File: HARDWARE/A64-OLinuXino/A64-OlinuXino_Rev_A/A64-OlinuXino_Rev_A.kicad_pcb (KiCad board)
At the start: 6 copper layers, 90 x 62.5 mm, 396 parts, among them Q1 E4SB25.000F20E15(25MHz/20pF/2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, Q2 MC-306_32.768KHZ/SMD_8038/6pF, Q3 4SB24.000F20E15/5x3.2mm/20ppm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, T1 WPM1481(DFN2X2-6L), U1 AllWinner-A64(FBGA396), U10 NA(RCLAMP0524P(SLP2510P8)), U11 RTL8723BS(ComboModule), U12 RTL8211CL-GR(LQFP48), U13 MT3608(SOT23-6), U14 AXP803(QFN68_8x8mm), U15 AT24C16BN-SH(SO-8_150mil), U2 K4B4G1646D-BCK0(FBGA-96_256Mx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, U3 K4B4G1646D-BCK0(FBGA-96_256Mx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, U4 NA(H27UBG8T2BTR-BC(TSOP48)), U5 MTFC4GACAANA-4M_IT(TBGA100), U6 SY6280AAC(SOT23-5), U7 NA(RCLAMP0524P(SLP2510P8)), U8 NA(RCLAMP0524P(SLP2510P8)), U9 SY6280AAC(SOT23-5)

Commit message: A64-OLinuXino update
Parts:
- removed C196: 100nF, OLIMEX_RLC-FP:C_0402_5MIL_DWS
- removed CON: B4B-PH-K-S, OLIMEX_Connectors-FP:B4B-PH-K-S
- removed Case: Case_Value, OLIMEX_Cases-FP:HAMMOND_1593LBK_A10_LIME
- removed R100, R99: NA(2.2k), OLIMEX_RLC-FP:R_0402_5MIL_DWS
- removed RM8: RA1206_(4x0603)_4B8_22R, OLIMEX_RLC-FP:RA1206_(4X0603)_4B8_xx
- removed U15: AT24C16BN-SH(SO-8_150mil), OLIMEX_IC-FP:SO-8
- added C197: 100nF, OLIMEX_RLC-FP:C_0402_5MIL_DWS, B.Cu at (143.7, 70.2)
- added HSIC1: B4B-PH-K-S, OLIMEX_Connectors-FP:B4B-PH-K-S, F.Cu at (121.8, 45.0)
- added HSIC_E1: Opened, OLIMEX_Jumpers-FP:SJ, B.Cu at (119.5, 47.4)
- added R101: NA(2.2k), OLIMEX_RLC-FP:R_0402_5MIL_DWS, F.Cu at (154.6, 64.4)
- added R102: NA(2.2k), OLIMEX_RLC-FP:R_0402_5MIL_DWS, F.Cu at (154.6, 63.4)
- added R103: NA(100k), OLIMEX_RLC-FP:R_0402_5MIL_DWS, B.Cu at (125.3, 46.9)
- added R104: NA(10k), OLIMEX_RLC-FP:R_0402_5MIL_DWS, B.Cu at (124.5, 46.9)
- 5V_E1, C1, C10, C102, C103, C104, C109, C11, C110, C113, C114, C115, C116, C117, C118, C119, C12, C120, C121, C123, C125, C126, C127, C128, C13, C130, C132, C133, C134, C135, C137, C14, C142, C145, C148, C149, C15, C151, C152, C153, C155, C156, C157, C158, C159, C16, C160, C161, C162, C163, C164, C165, C166, C167, C168, C17, C170, C171, C173, C174, C176, C177, C178, C179, C18, C180, C181, C183, C184, C186, C188, C189, C19, C190, C191, C192, C194, C195, C2, C20, C21, C22, C23, C24, C25, C26, C27, C28, C29, C3, C30, C31, C34, C35, C36, C37, C38, C4, C42, C43, C44, C46, C49, C5, C50, C51, C53, C54, C55, C56, C6, C61, C63, C64, C7, C72, C73, C79, C8, C80, C82, C88, C9, C96, C98, C99, D1, D3, D4, EMMC_PWR1, FET1, FET2, FUSE1, FUSE2, L1, L13, L2, Q1, Q2, R2, R3, R36, R37, R38, R4, R41, R42, R60, R61, R93, R96, R97, RM1, RM10, RM12, RM14, RM2, RM3, RM4, RM5, RM7, T1, VCC-PE:2.8V/3.3V1: moved to B.Cu
- NAND_E1: value Closed -> Soldered; moved to B.Cu
- PWRON1, RESET1, UBOOT1: footprint OLIMEX_Buttons-FP:WS_TAKT_6X3,5_SMD_NOCREAM -> OLIMEX_Buttons-FP:uTACTIL
- R1, R10, R11, R12, R14, R16, R17, R19, R20, R22, R24, R25, R26, R27, R28, R29, R32, R34, R35, R47, R48, R49, R50, R51, R52, R53, R55, R56, R57, R6, R63, R64, R65, R67, R7, R80, R81: footprint OLIMEX_RLC-FP:R_0603_5MIL_DWS -> OLIMEX_RLC-FP:R_0402_5MIL_DWS
- R13, R15, R21, R23, R30, R31, R46, R5, R58, R59, R66, R68, R69, R70, R71, R72, R73, R75, R76, R77, R79, R8, R83, R84, R85, R86, R87, R88, R89, R9, R90, R91, R92, R95: footprint OLIMEX_RLC-FP:R_0603_5MIL_DWS -> OLIMEX_RLC-FP:R_0402_5MIL_DWS; moved to B.Cu
- R74, R82: value 1k -> 2.2k; footprint OLIMEX_RLC-FP:R_0603_5MIL_DWS -> OLIMEX_RLC-FP:R_0402_5MIL_DWS
- R78: footprint OLIMEX_RLC-FP:R_0603_5MIL_DWS -> OLIMEX_RLC-FP:R_1206_5MIL_DWS; moved to B.Cu
- UEXT1: footprint OLIMEX_Connectors-FP:GBH-254-SMT-10 -> OLIMEX_Connectors-FP:HN2x5
- moved L5 502.1 mm to (113.5, 79.8), turned to 180 degrees
- moved R31 499.2 mm to (116.8, 84.5)
- moved C64 498.6 mm to (116.7, 87.1), turned to 270 degrees
- moved L2 490.2 mm to (118.6, 87.1), turned to 90 degrees
- moved R25 487.1 mm to (112.8, 88.6), turned to 90 degrees
- moved C58 485.1 mm to (114.3, 92.1)
- moved C62 480.2 mm to (115.3, 90.9)
- moved C51 475.8 mm to (137.5, 72.1), turned to 270 degrees
- moved R28 474.1 mm to (116.8, 90.6), turned to 270 degrees
- moved R26 473.9 mm to (113.3, 90.0), turned to 180 degrees
- moved R24 471.5 mm to (136.5, 52.3), turned to 90 degrees
- moved C48 471.0 mm to (113.3, 90.9)
- moved R19 469.1 mm to (136.8, 46.8), turned to 180 degrees
- moved C52 467.3 mm to (113.8, 88.6), turned to 90 degrees
- moved C66 466.5 mm to (116.6, 71.4), turned to 270 degrees
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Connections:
- net /S0SCKN renamed /S0SCK_N
- net /S0SCKP renamed /S0SCK_P
- net /S0SDQS0N renamed /S0SDQS0_N
- net /S0SDQS0P renamed /S0SDQS0_P
- net /S0SDQS1N renamed /S0SDQS1_N
- net /S0SDQS1P renamed /S0SDQS1_P
- net /S0SDQS2N renamed /S0SDQS2_N
- net /S0SDQS2P renamed /S0SDQS2_P
- net /S0SDQS3N renamed /S0SDQS3_N
- net /S0SDQS3P renamed /S0SDQS3_P
- RM10 pad 1.1: Net-(R53-Pad2) -> Net-(RM10-Pad1.1)
- RM10 pad 3.1: Net-(RM10-Pad3.1) -> Net-(R53-Pad2)
- RM11 pad 1.1: Net-(RM11-Pad1.1) -> Net-(RM10-Pad2.1)
- RM11 pad 1.2: /USB&HDMI,WiFi&BT,Ethernet,LCD/GRXD0/LCD_D15 -> /USB&HDMI,WiFi&BT,Ethernet,LCD/GRXD2/LCD_D13
- RM11 pad 2.1: Net-(R53-Pad2) -> Net-(RM11-Pad2.1)
- RM11 pad 2.2: /USB&HDMI,WiFi&BT,Ethernet,LCD/GRXD1/LCD_D14 -> /USB&HDMI,WiFi&BT,Ethernet,LCD/GRXD0/LCD_D15
- RM11 pad 3.1: Net-(RM10-Pad2.1) -> Net-(R53-Pad2)
- RM11 pad 3.2: /USB&HDMI,WiFi&BT,Ethernet,LCD/GRXD2/LCD_D13 -> /USB&HDMI,WiFi&BT,Ethernet,LCD/GRXD1/LCD_D14
- RM11 pad 4.1: Net-(RM10-Pad3.1) -> Net-(RM10-Pad1.1)
- RM13 pad 1.1: Net-(RM10-Pad4.1) -> Net-(C88-Pad2)
- RM13 pad 1.2: /USB&HDMI,WiFi&BT,Ethernet,LCD/GRXCTL/LCD_D19 -> /USB&HDMI,WiFi&BT,Ethernet,LCD/GRXCK/LCD_D18
- RM13 pad 2.1: Net-(C88-Pad2) -> Net-(RM10-Pad4.1)
- RM13 pad 2.2: /USB&HDMI,WiFi&BT,Ethernet,LCD/GRXCK/LCD_D18 -> /USB&HDMI,WiFi&BT,Ethernet,LCD/GRXCTL/LCD_D19
- RM3 pad 1.1: /NAND Flash , eMMC, T-Card and Audio/NAND0-DQ4/SDC2-D4 -> /NAND Flash , eMMC, T-Card and Audio/NAND0-DQ7/SDC2-D7
- RM3 pad 4.1: /NAND Flash , eMMC, T-Card and Audio/NAND0-DQ7/SDC2-D7 -> /NAND Flash , eMMC, T-Card and Audio/NAND0-DQ4/SDC2-D4
- RM5 pad 1.1: /NAND Flash , eMMC, T-Card and Audio/NAND0-RE/SDC2-CLK -> (no net)
- RM5 pad 1.2: Net-(EMMC1-Pad4) -> (no net)
- RM5 pad 2.1: /NAND Flash , eMMC, T-Card and Audio/NAND0-RB0/SDC2-CMD -> /NAND Flash , eMMC, T-Card and Audio/NAND0-DQS/SDC2-RST
- RM5 pad 2.2: Net-(EMMC1-Pad6) -> Net-(EMMC1-Pad8)
- RM5 pad 3.1: /NAND Flash , eMMC, T-Card and Audio/NAND0-DQS/SDC2-RST -> /NAND Flash , eMMC, T-Card and Audio/NAND0-RE/SDC2-CLK
- RM5 pad 3.2: Net-(EMMC1-Pad8) -> Net-(EMMC1-Pad4)
- RM5 pad 4.1: (no net) -> /NAND Flash , eMMC, T-Card and Audio/NAND0-RB0/SDC2-CMD
- RM5 pad 4.2: (no net) -> Net-(EMMC1-Pad6)
- RM6 pad 3.1: (no net) -> /NAND Flash , eMMC, T-Card and Audio/HPOUTR
- RM6 pad 3.2: (no net) -> Net-(C66-Pad2)
- U12 pad 14: Net-(RM11-Pad1.1) -> Net-(RM11-Pad2.1)
- U12 pad 18: Net-(RM10-Pad3.1) -> Net-(RM10-Pad1.1)
- U14 pad 8: Net-(L19-Pad1) -> +1.5V
- U14 pad 9: Net-(L20-Pad1) -> 1.1V_SYS
- U2 pad A2: /S0SDQ13 -> /S0SDQ15
- U2 pad A3: /S0SDQ15 -> /S0SDQ12
- U2 pad A7: /S0SDQ12 -> /S0SDQ8
- U2 pad B8: /S0SDQ14 -> /S0SDQ10
- U2 pad C2: /S0SDQ11 -> /S0SDQ13
- U2 pad C3: /S0SDQ9 -> /S0SDQ14
- U2 pad C8: /S0SDQ10 -> /S0SDQ9
- U2 pad D7: /S0SDQ8 -> /S0SDQ11
- U2 pad E3: /S0SDQ0 -> /S0SDQ4
- U2 pad F7: /S0SDQ1 -> /S0SDQ0
- U2 pad F8: /S0SDQ3 -> /S0SDQ7
- U2 pad G2: /S0SDQ6 -> /S0SDQ1
- U2 pad H3: /S0SDQ4 -> /S0SDQ5
- U2 pad H7: /S0SDQ7 -> /S0SDQ3
- U2 pad H8: /S0SDQ5 -> /S0SDQ6
- U3 pad A2: /S0SDQ29 -> /S0SDQ30
- U3 pad A3: /S0SDQ31 -> /S0SDQ28
- U3 pad A7: /S0SDQ28 -> /S0SDQ24
- U3 pad B8: /S0SDQ30 -> /S0SDQ27
- U3 pad C2: /S0SDQ27 -> /S0SDQ31
- U3 pad C3: /S0SDQ25 -> /S0SDQ29
- U3 pad C8: /S0SDQ26 -> /S0SDQ25
- U3 pad D7: /S0SDQ24 -> /S0SDQ26
- U3 pad E3: /S0SDQ16 -> /S0SDQ22
- U3 pad F2: /S0SDQ18 -> /S0SDQ21
- U3 pad F7: /S0SDQ17 -> /S0SDQ16
- U3 pad G2: /S0SDQ22 -> /S0SDQ23
- U3 pad H7: /S0SDQ23 -> /S0SDQ18
- U3 pad H8: /S0SDQ21 -> /S0SDQ17
- U5 pad K9: Net-(RM3-Pad4.2) -> Net-(RM3-Pad1.2)
- U5 pad N8: Net-(RM3-Pad1.2) -> Net-(RM3-Pad4.2)
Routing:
- net GND: track 0.00 -> 259.1 mm, vias 0 -> 147
- net +5V: track 0.00 -> 79.0 mm, vias 0 -> 1
- net AP-RESET#: track 0.00 -> 75.8 mm, vias 0 -> 4
- net Net-(R86-Pad1): track 0.00 -> 66.5 mm, vias 0 -> 1
- net Net-(R87-Pad1): track 0.00 -> 66.3 mm, vias 0 -> 1
- net +1.5V: track 0.00 -> 66.1 mm, vias 0 -> 41
- net /USB&HDMI,WiFi&BT,Ethernet,LCD/BT-RST-N: track 0.00 -> 61.8 mm, vias 0 -> 2
- net /USB&HDMI,WiFi&BT,Ethernet,LCD/WL-PMU-EN: track 0.00 -> 61.1 mm, vias 0 -> 3
- net /USB&HDMI,WiFi&BT,Ethernet,LCD/AP-WAKE-BT: track 0.00 -> 60.7 mm, vias 0 -> 3
- net /USB&HDMI,WiFi&BT,Ethernet,LCD/BT-WAKE-AP: track 0.00 -> 56.9 mm, vias 0 -> 3
- net AP-NMI#: track 0.00 -> 55.1 mm, vias 0 -> 4
- net AP-CK32KO: track 0.00 -> 54.1 mm, vias 0 -> 3
- net /S0SRST: track 0.00 -> 52.2 mm, vias 0 -> 2
- net /USB&HDMI,WiFi&BT,Ethernet,LCD/WL-WAKE-AP: track 0.00 -> 52.1 mm, vias 0 -> 3
- net /S0SBA1: track 0.00 -> 51.7 mm, vias 0 -> 3
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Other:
- net class Default: clearance 0.2 -> 0.127; trace_width 0.25 -> 0.127; via_dia 0.6 -> 0.327; via_drill 0.4 -> 0.2
- rule trace_clearance: 0.2 -> 0.127
- rule trace_min: 0.2 -> 0.1066
- rule via_min_drill: 0.3 -> 0.2
- rule via_min_size: 0.4 -> 0.327

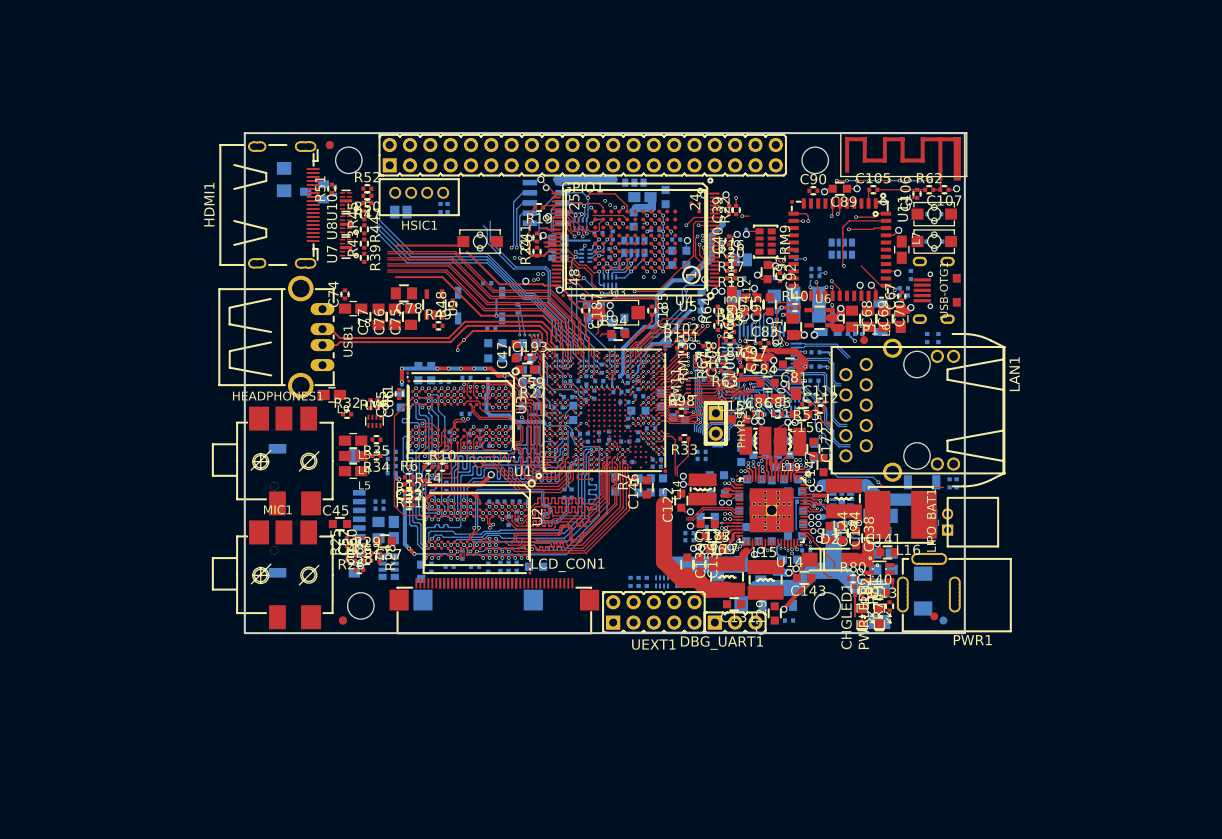
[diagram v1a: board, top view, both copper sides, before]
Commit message: A64-OLinuXino routing completed
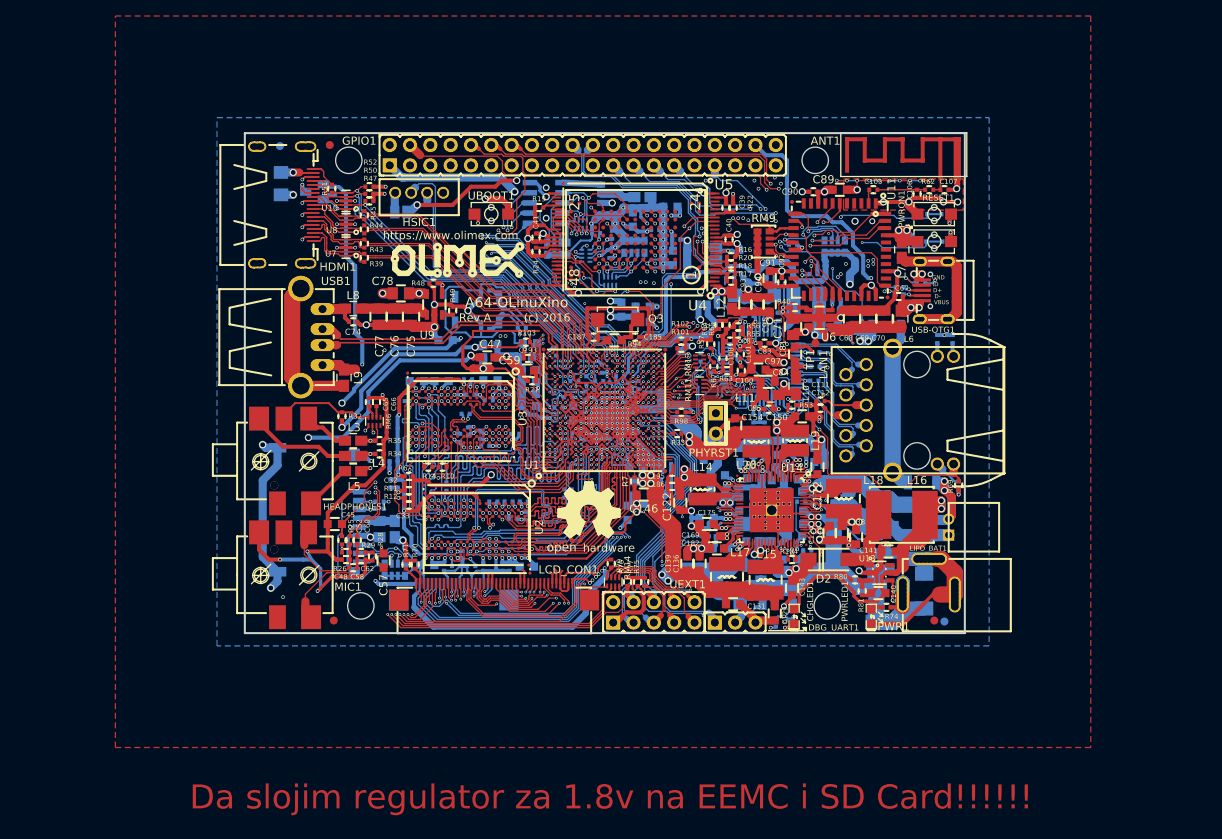
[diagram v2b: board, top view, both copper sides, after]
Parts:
- removed VCC-PE:2.8V/3.3V1: Closed(1-2);Opened(2-3), OLIMEX_Jumpers-FP:SJ_2_SMALL_12_TIED
- added 3.3V/VCC-PE:2.8V1: Opened(2-3);Closed(1-2), OLIMEX_Jumpers-FP:SJ_2_SMALL_12_TIED, B.Cu at (157.9, 58.9)
- added ?: , OLIMEX_LOGOs-FP:LOGO_ROHS_1, B.Cu at (123.2, 55.2)
- added ?: , OLIMEX_LOGOs-FP:LOGO_OPENHARDWARE_8x8, F.Cu at (143.0, 85.1)
- added ?: , OLIMEX_LOGOs-FP:LOGO_PBFREE, B.Cu at (141.5, 97.0)
- added ?: , OLIMEX_LOGOs-FP:LOGO_RECYCLEBIN_1, B.Cu at (149.5, 94.1)
- added ?: , OLIMEX_LOGOs-FP:OLIMEX_LOGO_TB, F.Cu at (126.7, 53.3)
- added ?: , OLIMEX_LOGOs-FP:LOGO_ANTISTATIC_1, B.Cu at (172.3, 48.9)
- C147, C86, R1, R82: moved to B.Cu
- C186, C195, R103, R104, R69, R70, R71, R75, R76, R77, R79, RM14: moved to F.Cu
- USB-OTG1: footprint OLIMEX_Connectors-FP:USB-MICRO-5P-F -> OLIMEX_Connectors-FP:USB-MICRO_MISB-SWMM-5B_LF
- moved R104 62.1 mm to (168.4, 90.8), turned to 180 degrees
- moved C15 20.8 mm to (130.5, 70.9), turned to 180 degrees
- moved R103 19.4 mm to (135.1, 63.6), turned to 0 degrees
- moved C190 18.9 mm to (125.1, 63.4), turned to 0 degrees
- moved C166 9.75 mm to (158.2, 78.4), turned to 180 degrees
- moved C163 9.49 mm to (157.5, 76.8)
- moved C21 9.04 mm to (130.7, 68.4), turned to 180 degrees
- moved R82 8.69 mm to (168.5, 98.7)
- moved R79 8.57 mm to (145.8, 91.3)
- moved CHGLED1 8.51 mm to (168.7, 97.9)
- moved ? 7.88 mm to (104.4, 98.6)
- moved ? 6.22 mm to (104.4, 39.1)
- moved TP1 6.11 mm to (171.3, 63.8)
- moved C120 6.10 mm to (149.7, 59.2), turned to 0 degrees
- moved RM14 6.10 mm to (146.1, 93.6), turned to 180 degrees
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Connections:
- MIPI-DSI1 pad 10: GND -> /Power Supply, Extensions and MiPi-DSI/DSI-D1N
- MIPI-DSI1 pad 11: /Power Supply, Extensions and MiPi-DSI/DSI-CKN -> /Power Supply, Extensions and MiPi-DSI/DSI-D1P
- MIPI-DSI1 pad 12: /Power Supply, Extensions and MiPi-DSI/DSI-D1N -> GND
- MIPI-DSI1 pad 13: /Power Supply, Extensions and MiPi-DSI/DSI-CKP -> /Power Supply, Extensions and MiPi-DSI/DSI-D2N
- MIPI-DSI1 pad 14: /Power Supply, Extensions and MiPi-DSI/DSI-D1P -> /Power Supply, Extensions and MiPi-DSI/DSI-D2P
- MIPI-DSI1 pad 16: GND -> /Power Supply, Extensions and MiPi-DSI/DSI-D3N
- MIPI-DSI1 pad 17: /Power Supply, Extensions and MiPi-DSI/DSI-D3N -> /Power Supply, Extensions and MiPi-DSI/DSI-D3P
- MIPI-DSI1 pad 18: /Power Supply, Extensions and MiPi-DSI/DSI-D2N -> GND
- MIPI-DSI1 pad 19: /Power Supply, Extensions and MiPi-DSI/DSI-D3P -> /Power Supply, Extensions and MiPi-DSI/DSI-CKN
- MIPI-DSI1 pad 20: /Power Supply, Extensions and MiPi-DSI/DSI-D2P -> /Power Supply, Extensions and MiPi-DSI/DSI-CKP
- MIPI-DSI1 pad 3: /Power Supply, Extensions and MiPi-DSI/MIPI-DSI-RST -> GND
- MIPI-DSI1 pad 4: GND -> /Power Supply, Extensions and MiPi-DSI/MIPI-DSI-RST
- MIPI-DSI1 pad 5: /Power Supply, Extensions and MiPi-DSI/MIPI-DSI-BKL -> /Power Supply, Extensions and MiPi-DSI/MIPI-DSI-EN
- MIPI-DSI1 pad 6: /Power Supply, Extensions and MiPi-DSI/DSI-D0N -> /Power Supply, Extensions and MiPi-DSI/MIPI-DSI-BKL
- MIPI-DSI1 pad 7: /Power Supply, Extensions and MiPi-DSI/MIPI-DSI-EN -> /Power Supply, Extensions and MiPi-DSI/DSI-D0N
- RM12 pad 1.2: /USB&HDMI,WiFi&BT,Ethernet,LCD/WL-PMU-EN -> /USB&HDMI,WiFi&BT,Ethernet,LCD/BT-RST-N
- RM12 pad 2.2: /USB&HDMI,WiFi&BT,Ethernet,LCD/WL-SDIO-CMD -> /USB&HDMI,WiFi&BT,Ethernet,LCD/WL-PMU-EN
- RM12 pad 3.2: /USB&HDMI,WiFi&BT,Ethernet,LCD/BT-UART-RX -> /USB&HDMI,WiFi&BT,Ethernet,LCD/WL-SDIO-CMD
- RM12 pad 4.2: /USB&HDMI,WiFi&BT,Ethernet,LCD/BT-RST-N -> /USB&HDMI,WiFi&BT,Ethernet,LCD/BT-UART-RX
- RM14 pad 1.1: SPI0_MISO -> Net-(RM14-Pad1.1)
- RM14 pad 1.2: Net-(RM14-Pad1.2) -> SPI0_MISO
- RM14 pad 2.1: SPI0_CLK -> Net-(RM14-Pad2.1)
- RM14 pad 2.2: Net-(RM14-Pad2.2) -> SPI0_MOSI
- RM14 pad 3.2: SPI0_MOSI -> SPI0_CLK
- RM7 pad 1.2: /NAND Flash , eMMC, T-Card and Audio/SDC0-D2 -> /NAND Flash , eMMC, T-Card and Audio/SDC0-D0
- RM7 pad 2.2: /NAND Flash , eMMC, T-Card and Audio/SDC0-D0 -> /NAND Flash , eMMC, T-Card and Audio/SDC0-D1
- RM7 pad 3.2: /NAND Flash , eMMC, T-Card and Audio/SDC0-D1 -> /NAND Flash , eMMC, T-Card and Audio/SDC0-DET#
- RM7 pad 4.2: /NAND Flash , eMMC, T-Card and Audio/SDC0-DET# -> /NAND Flash , eMMC, T-Card and Audio/SDC0-D2
- UEXT1 pad 7: Net-(RM14-Pad1.2) -> Net-(RM14-Pad1.1)
- UEXT1 pad 8: Net-(RM14-Pad3.1) -> Net-(RM14-Pad2.1)
- UEXT1 pad 9: Net-(RM14-Pad2.2) -> Net-(RM14-Pad3.1)
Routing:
- net GND: track 259.1 -> 1572.2 mm, vias 147 -> 235
- net +3V3: track 39.9 -> 283.9 mm, vias 17 -> 28
- net +5V: track 79.0 -> 279.5 mm, vias 1 -> 11
- net SPI0_CLK: track 30.7 -> 179.1 mm, vias 2 -> 3
- net SPI0_MOSI: track 26.8 -> 173.9 mm, vias 2 -> 3
- net SPI0_MISO: track 37.4 -> 181.8 mm, vias 3 -> 4
- net SPI0_CS: track 31.5 -> 173.6 mm, vias 2 -> 3
- net +3.3VD: track 21.6 -> 160.3 mm, vias 3 -> 6
- net +1.5V: track 66.1 -> 196.4 mm, vias 41 -> 51
- net +3.0VA: track 13.6 -> 138.7 mm, vias 4 -> 6
- net 3.0V_RTC: track 23.6 -> 142.0 mm, vias 4 -> 5
- net +1V8: track 35.5 -> 153.5 mm, vias 3 -> 5
- net PMU-SDA: track 43.3 -> 158.2 mm, vias 3 -> 4
- net 1.2V_HSIC: track 41.3 -> 150.9 mm, vias 4 -> 8
- net GNDA: track 3.60 -> 112.0 mm, vias 2 -> 7
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- added copper zone on In4.Cu, net +1.5V
- added copper zone on In4.Cu, net +3V3
- added copper zone on In4.Cu, net 1.1V_CPUX
- added copper zone on In4.Cu, net 1.1V_SYS
- added copper zone on B.Cu, net GND
- added copper zone on F.Cu, net GND
- added copper zone on In1.Cu, net GND
- added copper zone on In2.Cu, net GND
- added copper zone on In3.Cu, net GND
- added copper zone on In4.Cu, net GND
- added copper zone on In4.Cu, net IPS
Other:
- rule trace_min: 0.1066 -> 0.1016
- board text added: "(c) 2016"
- board text added: "A64-OLinuXino"
- board text added: "Da slojim regulator za 1.8v na EEMC i SD Card!!!!!!"
- board text added: "Rev.A"
- board text added: "https://www.olimex.com"
